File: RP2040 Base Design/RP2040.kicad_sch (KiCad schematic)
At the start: 27 parts, among them J1 USB_B_Micro, J2 Conn_01x02, J3 RP2040_SWD, U1 RP2040, U2 AMS1117-3.3, U3 W25Q128JVS, Y1 X322512MSB4SI

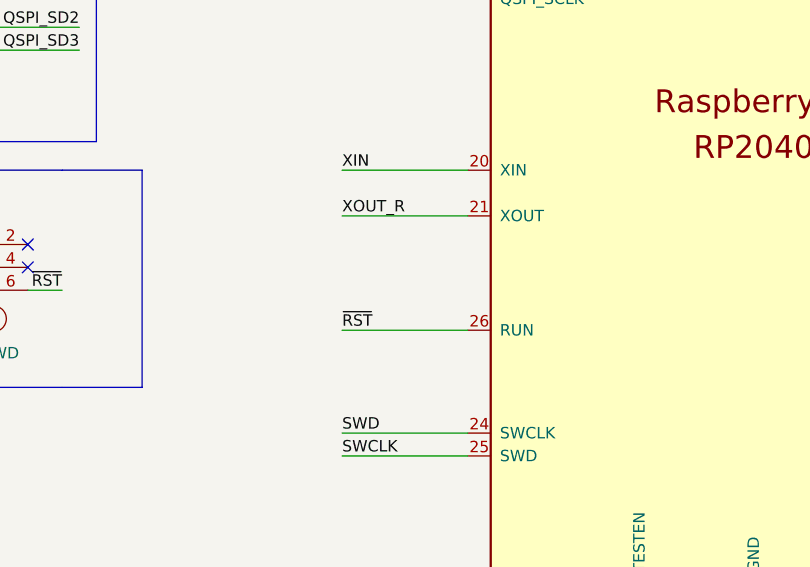
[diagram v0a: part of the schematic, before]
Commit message: Add 10k pullup resistor to RUN pin for debugging Fixes #2
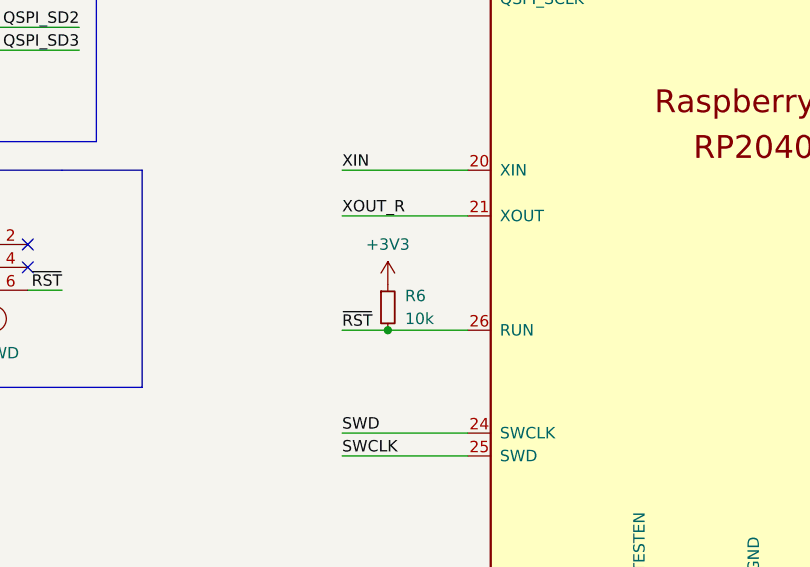
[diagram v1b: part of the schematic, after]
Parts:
- added R6: 10k, Custom_Footprints:Perfect_0402, symbol Device:R_Small
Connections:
- net +3V3: now also R6.1
- net ~{RST}: now also R6.2
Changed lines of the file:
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@@
   (junction (at 139.065 29.845) (diameter 0) (color 0 0 0 0)
+  )
+  (junction (at 137.795 123.825) (diameter 0) (color 0 0 0 0)
   )
   (junction (at 179.705 40.005) (diameter 0) (color 0 0 0 0)
@@
     (stroke (width 0) (type default) (color 0 0 0 0))
   )
+  (wire (pts (xy 137.795 123.825) (xy 146.685 123.825))
+    (stroke (width 0) (type default) (color 0 0 0 0))
+  )
   (wire (pts (xy 210.185 80.645) (xy 225.425 80.645))
     (stroke (width 0) (type default) (color 0 0 0 0))
@@
     (stroke (width 0) (type default) (color 0 0 0 0))
   )
+  (wire (pts (xy 132.715 123.825) (xy 137.795 123.825))
+    (stroke (width 0) (type default) (color 0 0 0 0))
+  )
   (wire (pts (xy 29.21 29.21) (xy 38.1 29.21))
     (stroke (width 0) (type default) (color 0 0 0 0))
@@
   )
   (wire (pts (xy 210.185 141.605) (xy 225.425 141.605))
-    (stroke (width 0) (type default) (color 0 0 0 0))
-  )
-  (wire (pts (xy 146.685 123.825) (xy 132.715 123.825))
     (stroke (width 0) (type default) (color 0 0 0 0))
   )
@@
     (pin "9")
   )
+  (symbol (lib_id "power:+3V3") (at 137.795 118.745 0) (unit 1)
+    (in_bom yes) (on_board yes)
+    (property "Reference" "#PWR02" (id 0) (at 137.795 122.555 0)
+      (effects (font (size 1.27 1.27)) hide)
+    )
+    (property "Value" "+3V3" (id 1) (at 137.795 114.3 0))
+    (property "Footprint" "" (id 2) (at 137.795 118.745 0)
+      (effects (font (size 1.27 1.27)) hide)
+    )
+    (property "Datasheet" "" (id 3) (at 137.795 118.745 0)
+      (effects (font (size 1.27 1.27)) hide)
+    )
+    (pin "1")
+  )
   (symbol (lib_id "Device:R") (at 43.815 85.09 270) (unit 1)
     (in_bom yes) (on_board yes)
@@
       (effects (font (size 1.27 1.27)) hide)
     )
+    (pin "1")
+    (pin "2")
+  )
+  (symbol (lib_id "Device:R_Small") (at 137.795 121.285 0) (unit 1)
+    (in_bom yes) (on_board yes) (fields_autoplaced)
+    (property "Reference" "R6" (id 0) (at 139.7 120.0149 0)
+      (effects (font (size 1.27 1.27)) (justify left))
+    )
+    (property "Value" "10k" (id 1) (at 139.7 122.5549 0)
+      (effects (font (size 1.27 1.27)) (justify left))
+    )
+    (property "Footprint" "Custom_Footprints:Perfect_0402" (id 2) (at 137.795 121.285 0)
+      (effects (font (size 1.27 1.27)) hide)
+    )
+    (property "Datasheet" "~" (id 3) (at 137.795 121.285 0)
+      (effects (font (size 1.27 1.27)) hide)
+    )
+    (property "MPN - JLCPCB" "C25744" (id 4) (at 137.795 121.285 0)
+      (effects (font (size 1.27 1.27)) hide)
+    )

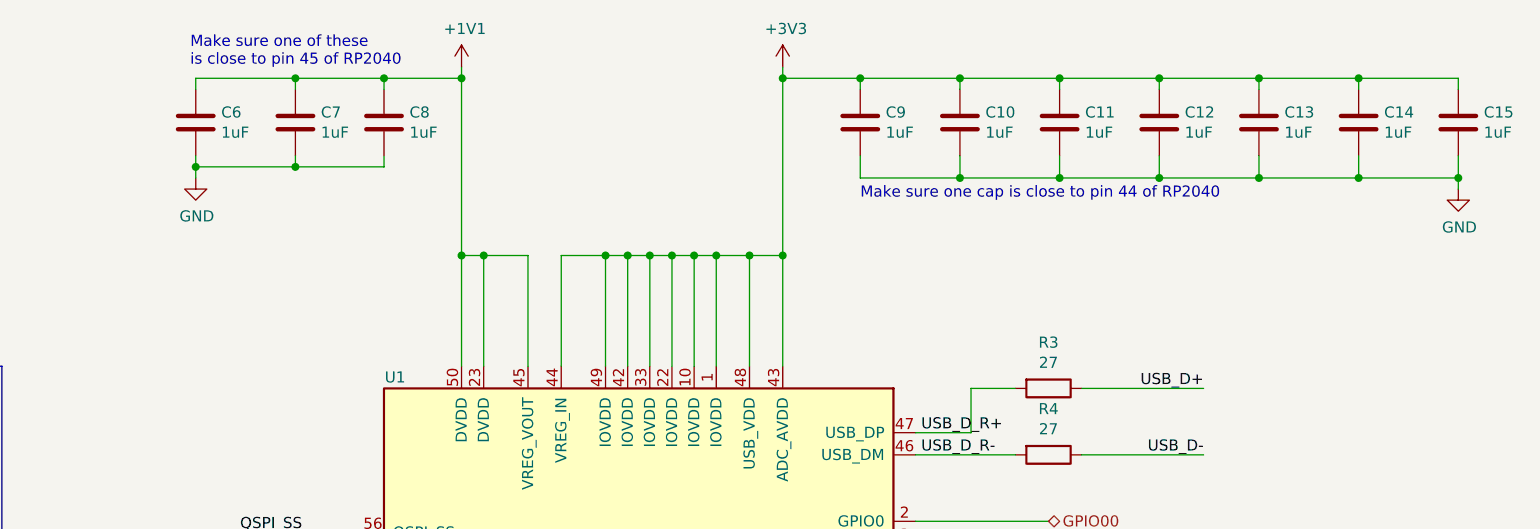
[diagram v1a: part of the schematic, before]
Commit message: Fixes Fix cap values #6
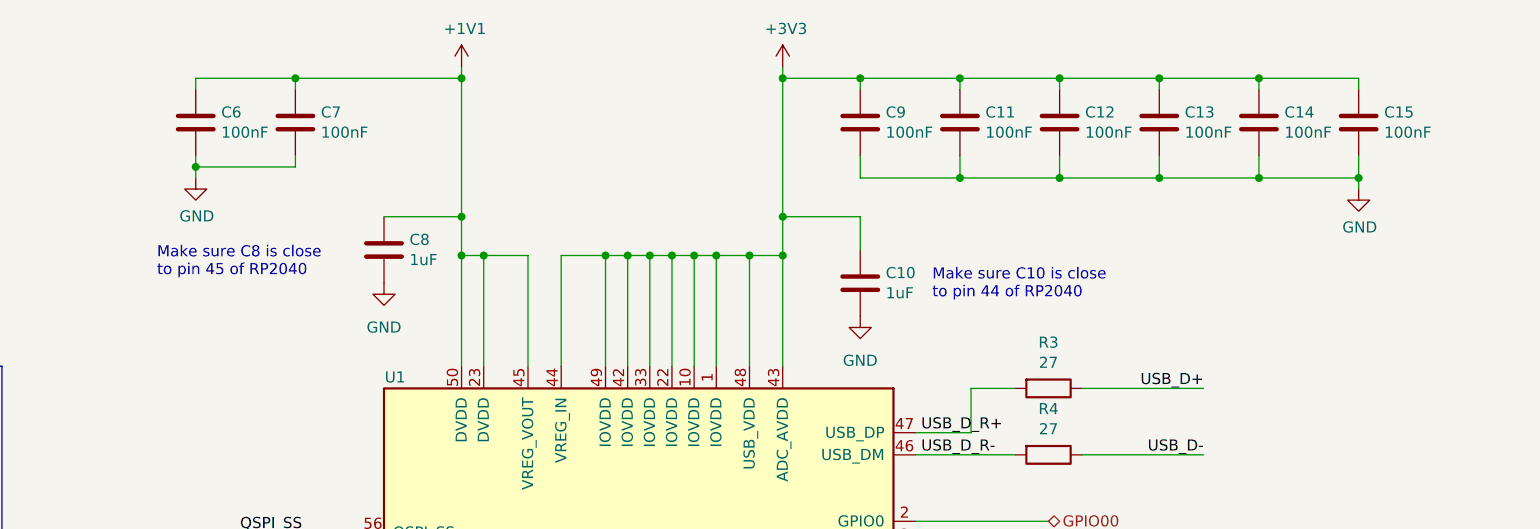
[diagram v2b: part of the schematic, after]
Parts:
- C11, C12, C13, C14, C15, C6, C7, C9: value 1uF -> 100nF; MPN - JLCPCB C52923 -> C1525
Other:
- note added: "Make sure C10 is close to pin 44 of RP2040"
- note added: "Make sure C8 is close to pin 45 of RP2040"
- note removed: "Make sure one cap is close to pin 44 of RP2040"
- note removed: "Make sure one of these is close to pin 45 of RP2040"
- moved on the sheet: C10, C11, C12, C13, C14, C15, C8
